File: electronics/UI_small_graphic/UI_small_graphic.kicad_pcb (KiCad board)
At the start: 2 copper layers, 2 parts

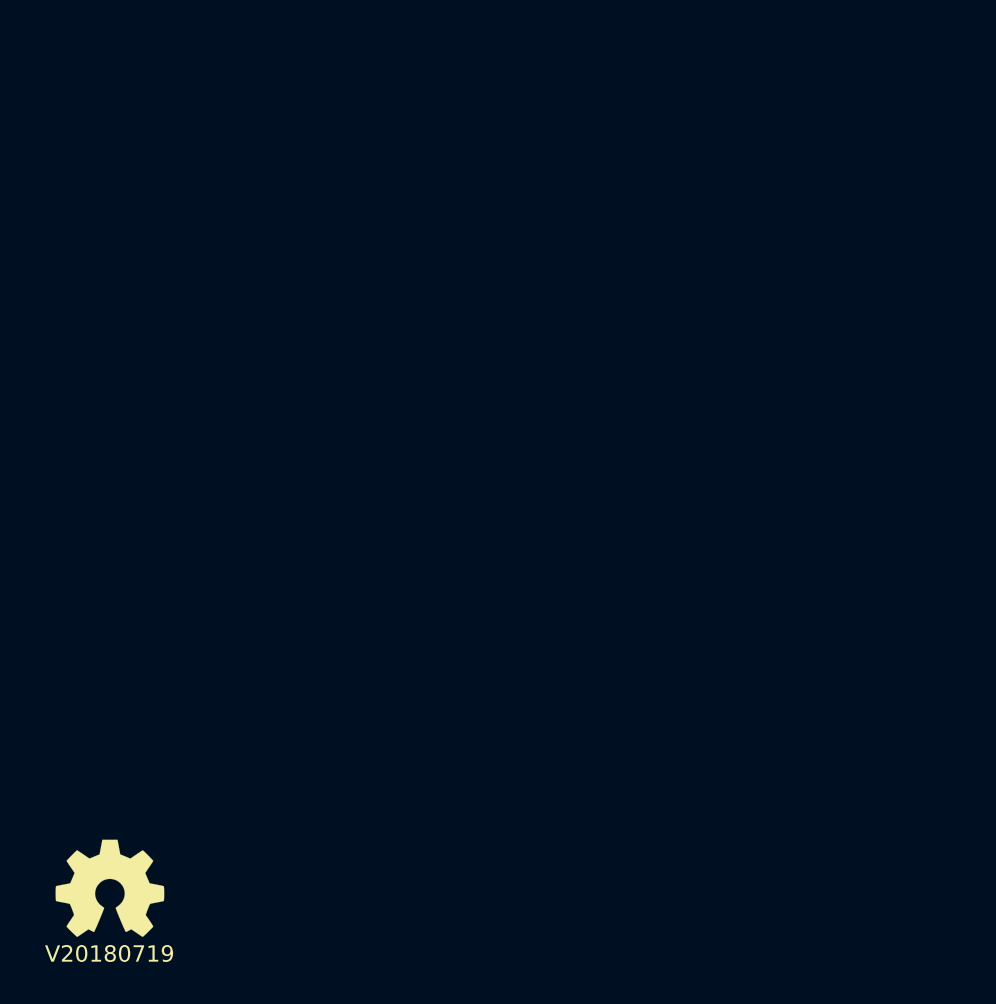
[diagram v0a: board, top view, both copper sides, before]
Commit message: started with PCB dimensions and input connector
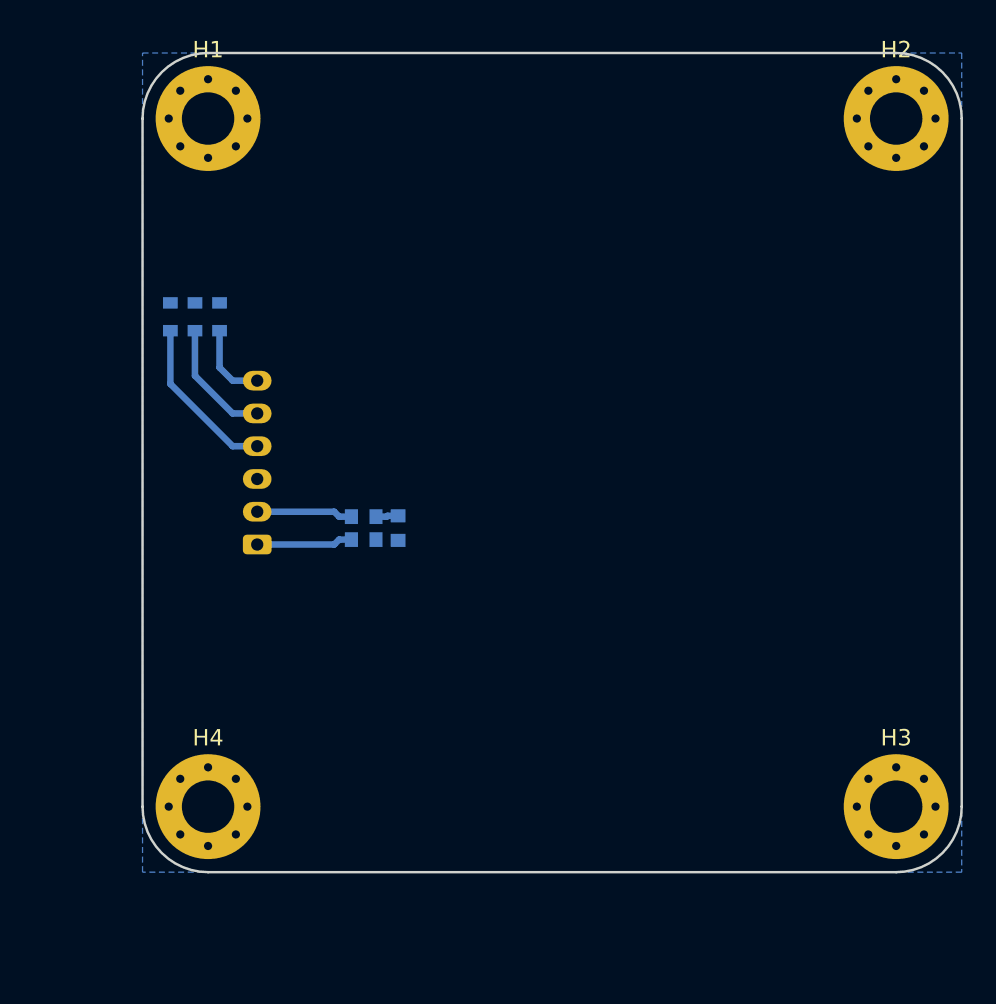
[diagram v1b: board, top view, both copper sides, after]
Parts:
- added C1: 10u, SquantorRcl:C_0603, B.Cu at (165.6, 79.0)
- added FB1: 600, SquantorRcl:L_0603, B.Cu at (163.5, 78.3)
- added FB2: 600, SquantorRcl:L_0603, B.Cu at (163.5, 79.7)
- added H1: MountingHole, MountingHole:MountingHole_3.2mm_M3_Pad_Via, F.Cu at (154.0, 54.0)
- added H2: MountingHole, MountingHole:MountingHole_3.2mm_M3_Pad_Via, F.Cu at (196.0, 54.0)
- added H3: MountingHole, MountingHole:MountingHole_3.2mm_M3_Pad_Via, F.Cu at (196.0, 96.0)
- added H4: MountingHole, MountingHole:MountingHole_3.2mm_M3_Pad_Via, F.Cu at (154.0, 96.0)
- added J1: Conn_01x06, Connector_JST:JST_PH_S6B-PH-K_1x06_P2.00mm_Horizontal, B.Cu at (157.0, 80.0)
- added R1: 100, SquantorRcl:R_0603_hand, B.Cu at (151.7, 66.1)
- added R2: 100, SquantorRcl:R_0603_hand, B.Cu at (153.2, 66.1)
- added R3: 100, SquantorRcl:R_0603_hand, B.Cu at (154.7, 66.1)
- N1: moved to B.Cu
- N2: value V20180719 -> V20220201; footprint SquantorLabels:Label_version -> SquantorLabels:Label_Generic; moved to B.Cu
- moved N2 30.8 mm to (177.5, 96.0), turned to 180 degrees
- moved N1 29.2 mm to (175.0, 90.0), turned to 180 degrees
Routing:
- net Net-(J1-Pad4): track 0.00 -> 10.1 mm
- net Net-(J1-Pad5): track 0.00 -> 7.50 mm
- net Net-(FB2-Pad2): track 0.00 -> 5.87 mm
- net Net-(FB1-Pad2): track 0.00 -> 5.87 mm
- net Net-(J1-Pad6): track 0.00 -> 4.88 mm
- net /3.3V: track 0.00 -> 1.37 mm
- added copper zone on B.Cu, net /VSS
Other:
- board outline added: 50 x 50 mm
- board text added: "!INT"
- board text added: "3.3V"
- board text added: "SCL"
- board text added: "SDA"
- board text added: "VSS"

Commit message: added displays to board
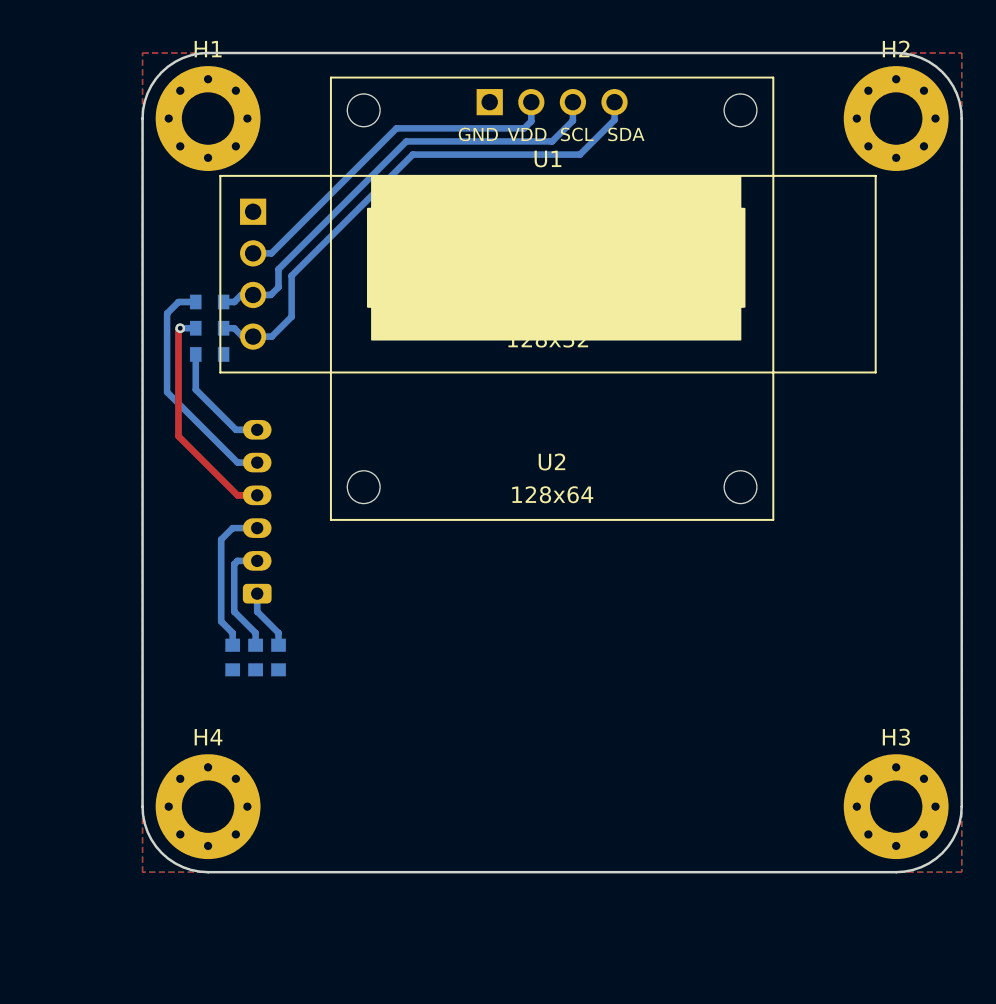
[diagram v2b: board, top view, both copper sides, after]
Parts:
- added U1: 128x32, SquantorModules:OLED_128x32, F.Cu at (174.8, 63.5)
- added U2: 128x64, SquantorModules:OLED_128x64, F.Cu at (175.0, 65.0)
- moved C1 12.8 mm to (155.5, 86.9), turned to 270 degrees
- moved FB1 10.8 mm to (156.9, 86.9), turned to 90 degrees
- moved FB2 8.88 mm to (158.3, 86.9), turned to 90 degrees
- moved J1 3.00 mm to (157.0, 83.0)
- moved R1 2.50 mm to (154.1, 66.8), turned to 180 degrees
- moved R3 2.38 mm to (154.1, 68.4), turned to 180 degrees
- moved R2 1.27 mm to (154.1, 65.2), turned to 180 degrees
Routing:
- net /SDA: track 0.00 -> 32.1 mm
- net /SCL: track 0.00 -> 27.7 mm
- net /3.3V: track 1.37 -> 21.5 mm
- net /VSS: track 0.00 -> 9.23 mm
- net Net-(J1-Pad5): track 7.50 -> 14.1 mm
- net Net-(J1-Pad4): track 10.1 -> 13.9 mm, vias 0 -> 1
- net Net-(FB2-Pad2): track 5.87 -> 3.69 mm
- net Net-(J1-Pad6): track 4.88 -> 6.91 mm
- net Net-(FB1-Pad2): track 5.87 -> 6.97 mm
- added copper zone on F.Cu, net /VSS

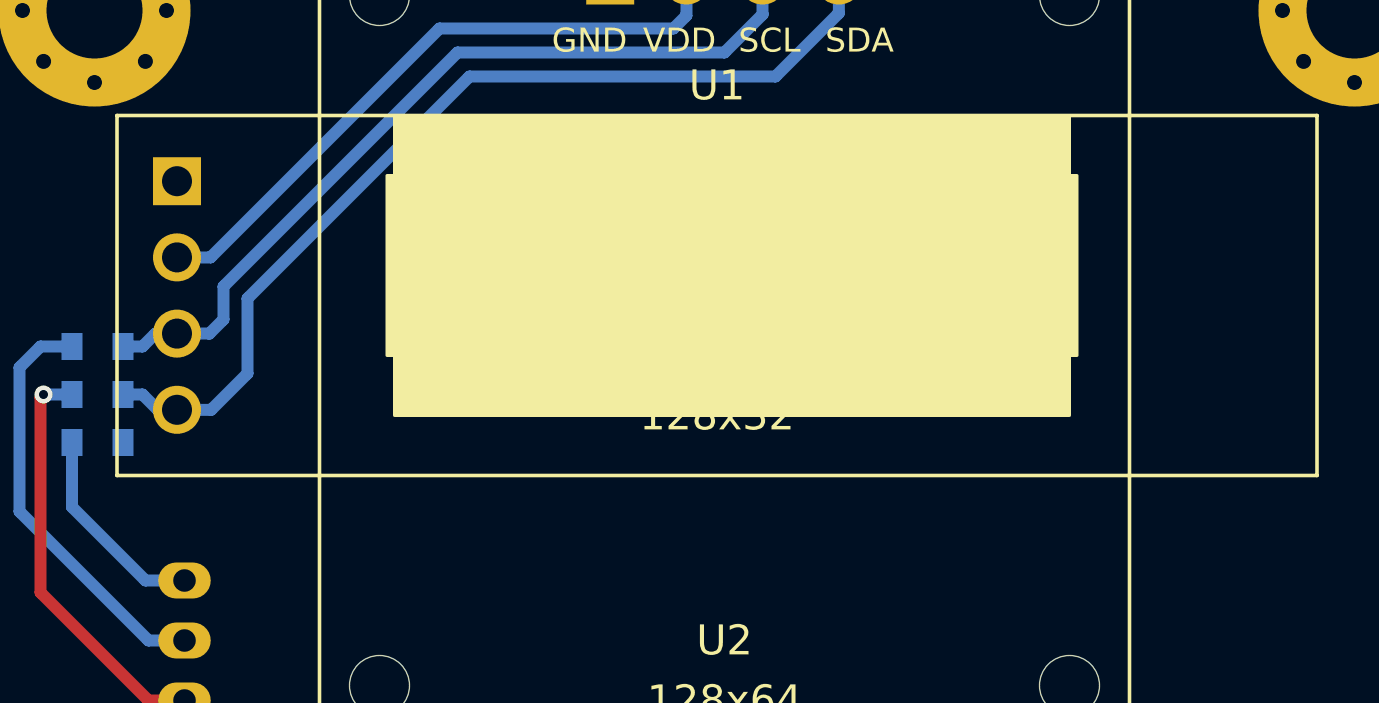
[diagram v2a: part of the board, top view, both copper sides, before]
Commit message: added I2C port expanders to PCB
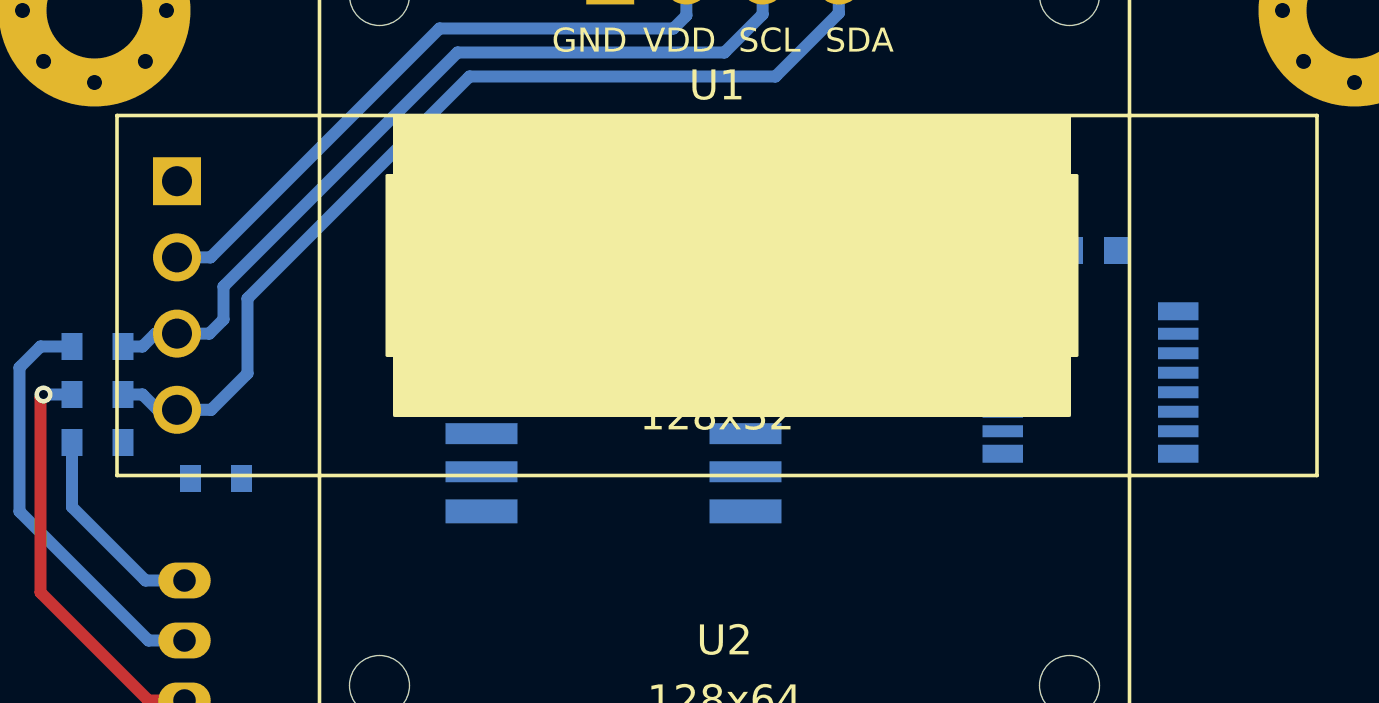
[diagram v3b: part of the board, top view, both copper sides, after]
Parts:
- added C2: 1u, SquantorRcl:C_0603, B.Cu at (187.3, 62.0)
- added C3: 1u, SquantorRcl:C_0603, B.Cu at (170.6, 60.1)
- added R4: 4.7K, SquantorRcl:R_0603_hand, B.Cu at (158.1, 69.6)
- added U3: PCF8574, SquantorIC:SOT162-1-NXP, B.Cu at (171.3, 66.2)
- added U4: PCA9554, SquantorIC:SOT403-1-NXP, B.Cu at (187.2, 66.4)

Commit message: routing
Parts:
- added C4: 100n, SquantorRcl:C_0603, B.Cu at (165.0, 96.0)
- added C5: 100n, SquantorRcl:C_0603, B.Cu at (178.0, 96.0)
- added C6: 100n, SquantorRcl:C_0603, B.Cu at (191.0, 96.0)
- added D1: SD05, SquantorDiodes:SOD_323_onsemi, B.Cu at (164.0, 98.0)
- added D2: SD05, SquantorDiodes:SOD_323_onsemi, B.Cu at (177.0, 98.0)
- added D3: SD05, SquantorDiodes:SOD_323_onsemi, B.Cu at (190.0, 98.0)
- added JP1: A0, SquantorSpecial:solder_jumper_0603_3way_12conn, B.Cu at (180.5, 69.8)
- added JP2: A1, SquantorSpecial:solder_jumper_0603_3way_12conn, B.Cu at (180.5, 68.0)
- added JP3: A2, SquantorSpecial:solder_jumper_0603_3way_12conn, B.Cu at (180.5, 66.1)
- added JP4: A0, SquantorSpecial:solder_jumper_0603_3way_12conn, B.Cu at (192.9, 69.0)
- added JP5: A1, SquantorSpecial:solder_jumper_0603_3way_12conn, B.Cu at (192.9, 67.2)
- added JP6: A2, SquantorSpecial:solder_jumper_0603_3way_12conn, B.Cu at (192.9, 65.4)
- added R10: 4.7K, SquantorRcl:R_0603_hand, B.Cu at (185.0, 96.0)
- added R5: 100, SquantorRcl:R_0603_hand, B.Cu at (162.0, 96.0)
- added R6: 4.7K, SquantorRcl:R_0603_hand, B.Cu at (159.0, 96.0)
- added R7: 100, SquantorRcl:R_0603_hand, B.Cu at (175.0, 96.0)
- added R8: 100, SquantorRcl:R_0603_hand, B.Cu at (188.0, 96.0)
- added R9: 4.7K, SquantorRcl:R_0603_hand, B.Cu at (172.0, 96.0)
- added S1: BUT0, SquantorSwitches:Omron_B3F-4055, F.Cu at (162.0, 87.0)
- added S2: BUT1, SquantorSwitches:Omron_B3F-4055, F.Cu at (175.0, 87.0)
- added S3: BUT2, SquantorSwitches:Omron_B3F-4055, F.Cu at (188.0, 87.0)
- moved C1 12.3 mm to (158.8, 75.0), turned to 0 degrees
- moved FB1 10.7 mm to (158.8, 76.4), turned to 180 degrees
- moved FB2 9.11 mm to (158.8, 77.8), turned to 180 degrees
- moved C3 8.42 mm to (179.0, 60.7), turned to 270 degrees
- moved R2 8.27 mm to (158.8, 72.0)
- moved R1 8.18 mm to (158.8, 73.5)
- moved N2 7.86 mm to (175.9, 88.3)
- moved N1 5.70 mm to (174.9, 84.3)
- moved R3 5.15 mm to (158.8, 70.5)
- moved J1 5.00 mm to (153.0, 80.0)
- moved C2 3.81 mm to (191.1, 62.2), turned to 270 degrees
- moved R4 3.76 mm to (161.7, 70.5)
- moved U3 2.20 mm to (172.4, 64.3), turned to 90 degrees
- moved U4 2.00 mm to (187.3, 64.4), turned to 90 degrees
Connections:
- net /BUTTON0 renamed /BUTT0
- net /BUTTON1 renamed /BUTT1
- net /BUTTON2 renamed /BUTT2
- net /BUTTON3 renamed /BUTT3
- U3 pad 10: /BUTTON4 -> Net-(U3-Pad10)
- U3 pad 11: /BUTTON4 -> Net-(U3-Pad11)
- U3 pad 9: /BUTTON4 -> Net-(U3-Pad9)
- U4 pad 10: /BUTTON4 -> Net-(U4-Pad10)
- U4 pad 11: /BUTTON4 -> Net-(U4-Pad11)
- U4 pad 9: /BUTTON4 -> Net-(U4-Pad9)
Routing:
- net /3.3V: track 21.5 -> 137.3 mm, vias 0 -> 5
- net /BUTT2: track 0.00 -> 58.3 mm, vias 0 -> 4
- net /BUTT0: track 0.00 -> 57.6 mm, vias 0 -> 4
- net /BUTT1: track 0.00 -> 54.7 mm, vias 0 -> 4
- net /SCL: track 27.7 -> 46.9 mm
- net Net-(R5-Pad1): track 0.00 -> 18.8 mm
- net Net-(R10-Pad2): track 0.00 -> 18.8 mm
- net Net-(R7-Pad1): track 0.00 -> 18.7 mm
- net /SDA: track 32.1 -> 46.2 mm
- net Net-(JP3-Pad2): track 0.00 -> 9.45 mm
- net Net-(J1-Pad5): track 14.1 -> 4.95 mm
- net Net-(J1-Pad4): track 13.9 -> 5.16 mm, vias 1 -> 0
- net Net-(JP2-Pad2): track 0.00 -> 7.66 mm
- net Net-(JP6-Pad2): track 0.00 -> 7.37 mm
- net /!INT: track 0.00 -> 7.33 mm, vias 0 -> 1
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
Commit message: further routing
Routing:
- net /BUZZ: track 0.00 -> 41.1 mm, vias 0 -> 4
- net /!INT: track 7.33 -> 43.5 mm, vias 1 -> 3
- net /3.3V: track 137.3 -> 164.1 mm, vias 5 -> 7
- net /BUTT3: track 0.00 -> 24.9 mm, vias 0 -> 4
- net /SCL: track 46.9 -> 63.7 mm, vias 0 -> 3
- net /SDA: track 46.2 -> 60.5 mm, vias 0 -> 3
- net /BUTT1: track 54.7 -> 55.6 mm
- net /BUTT0: track 57.6 -> 58.3 mm
- net /BUTT2: track 58.3 -> 58.9 mm
- net /VSS: vias 9 -> 22

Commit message: routing completed
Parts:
- added BZ1: Buzzer, Buzzer_Beeper:Buzzer_12x9.5RM7.6, B.Cu at (197.3, 72.9)
- added R11: TBD, SquantorRcl:R_0603_hand, B.Cu at (186.3, 69.1)
- moved JP4 4.66 mm to (189.1, 66.3)
- moved JP5 4.66 mm to (189.1, 64.5)
- moved JP6 4.66 mm to (189.1, 62.7)
- moved C2 3.85 mm to (187.6, 60.6)
- moved U4 3.40 mm to (183.9, 64.4)
- moved C3 2.83 mm to (177.0, 58.7)
- moved JP1 2.00 mm to (178.5, 69.8)
- moved JP2 2.00 mm to (178.5, 68.0)
- moved JP3 2.00 mm to (178.5, 66.1)
- moved U3 2.00 mm to (170.4, 64.3)
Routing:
- net /3.3V: track 164.1 -> 185.5 mm, vias 7 -> 5
- net Net-(BZ1-Pad2): track 0.00 -> 6.06 mm
- net /!INT: track 43.5 -> 37.8 mm
- net /BUZZ: track 41.1 -> 45.0 mm
- net /BUTT0: track 58.3 -> 55.4 mm
- net /VSS: track 5.04 -> 7.36 mm, vias 22 -> 24
- net /SDA: track 60.5 -> 62.1 mm
- net /BUTT3: track 24.9 -> 23.5 mm
- net /BUTT1: track 55.6 -> 54.2 mm
- net /BUTT2: track 58.9 -> 59.8 mm
- net Net-(JP4-Pad2): track 5.48 -> 4.59 mm

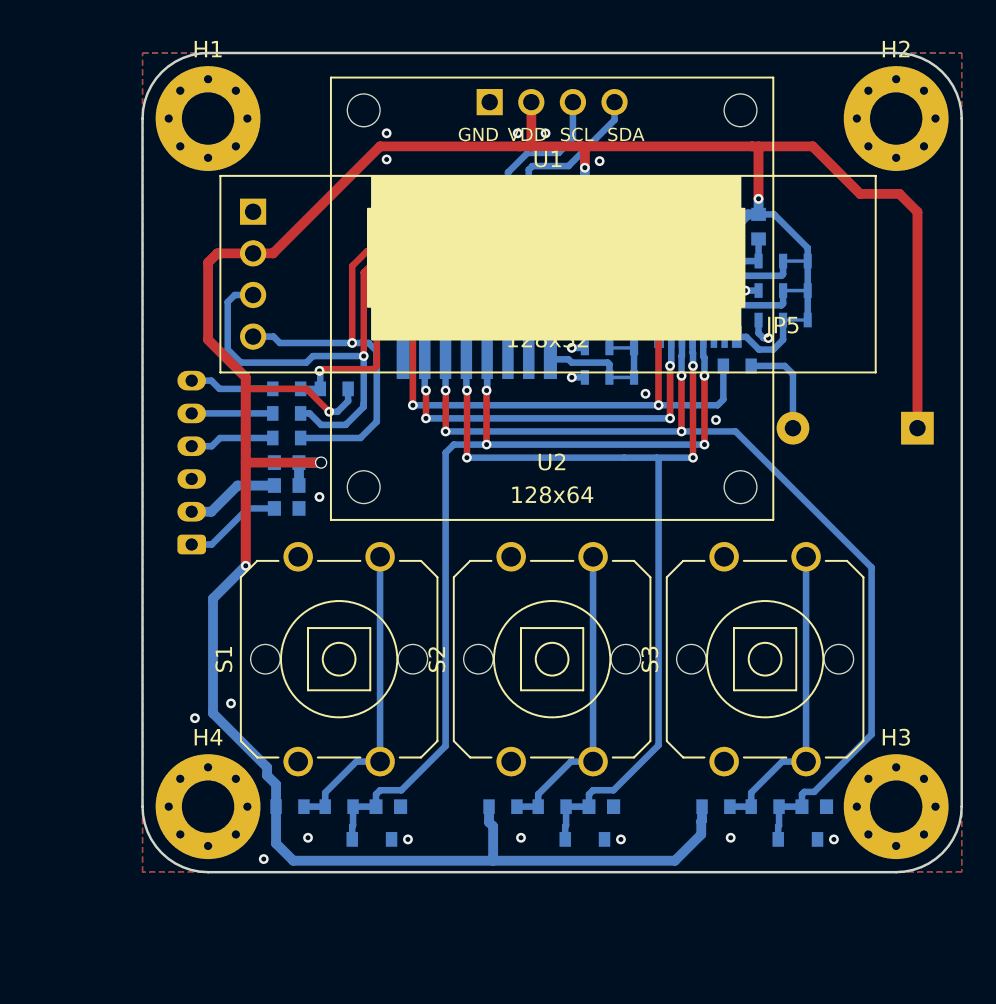
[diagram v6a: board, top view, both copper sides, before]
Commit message: routing completed, added decoupling caps for displays, started with silk placement
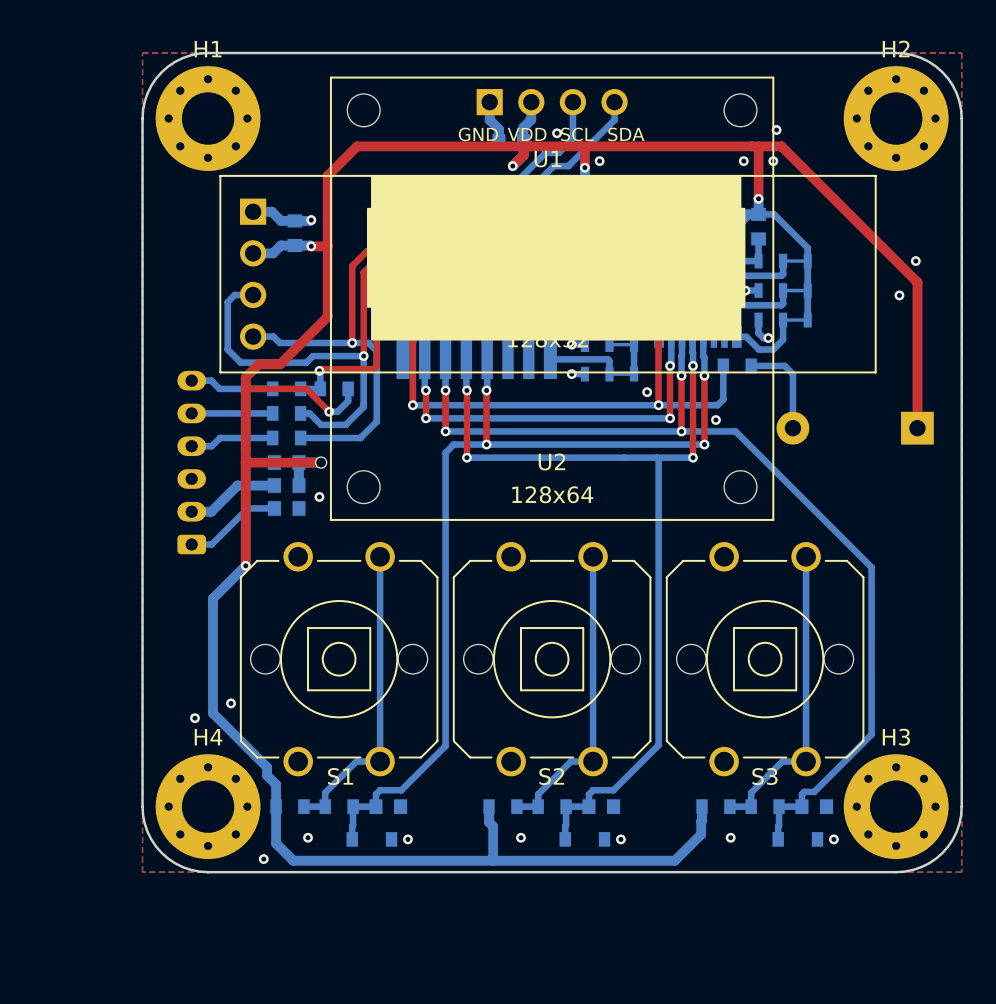
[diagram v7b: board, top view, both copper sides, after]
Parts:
- added C7: 10u, SquantorRcl:C_0603, B.Cu at (172.5, 55.4)
- added C8: 10u, SquantorRcl:C_0603, B.Cu at (159.3, 61.0)
- moved JP1 0.20 mm to (178.5, 69.6)
- moved JP2 0.20 mm to (178.5, 67.8)
- moved JP3 0.20 mm to (178.5, 65.9)
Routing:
- net /VSS: track 7.36 -> 39.9 mm, vias 24 -> 27
- net /3.3V: track 185.5 -> 187.7 mm, vias 5 -> 7
- net /SDA: track 62.1 -> 61.4 mm
- net /SCL: track 63.9 -> 63.3 mm

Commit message: added new versionnumber, updated silk placement top, WIP bottom
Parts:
- N2: value V20220201 -> V20220213
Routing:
- net /VSS: vias 27 -> 28
